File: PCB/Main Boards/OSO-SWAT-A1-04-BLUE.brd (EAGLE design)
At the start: 24.4 x 24.4 mm, 36 parts, among them J1 FH19C-9S-0.5SH_10_, U1 ATSAML22J18A-MUT, U2 MIC5365-3.3YC5-TR

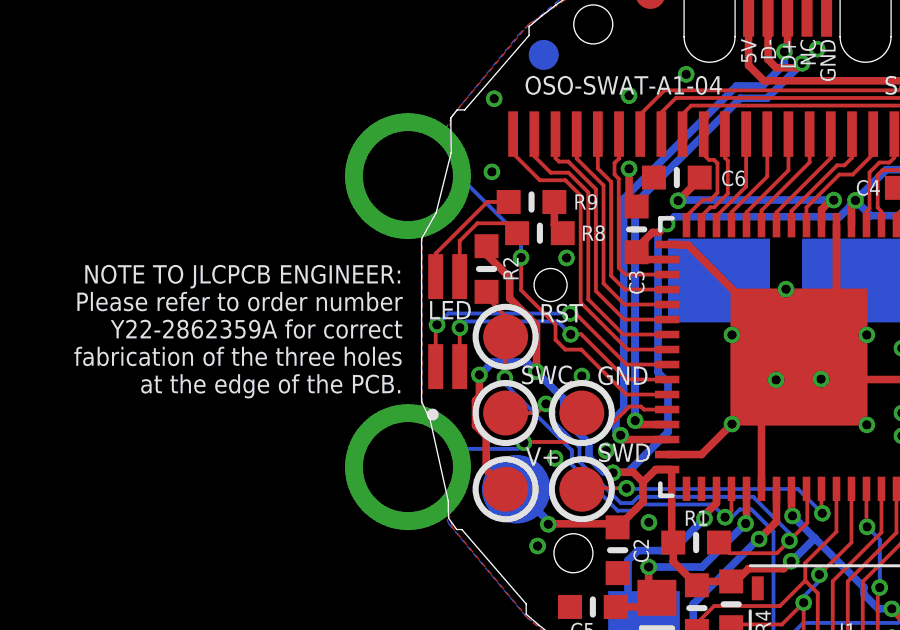
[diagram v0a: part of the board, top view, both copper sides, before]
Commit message: fix LED part number, make boards identical
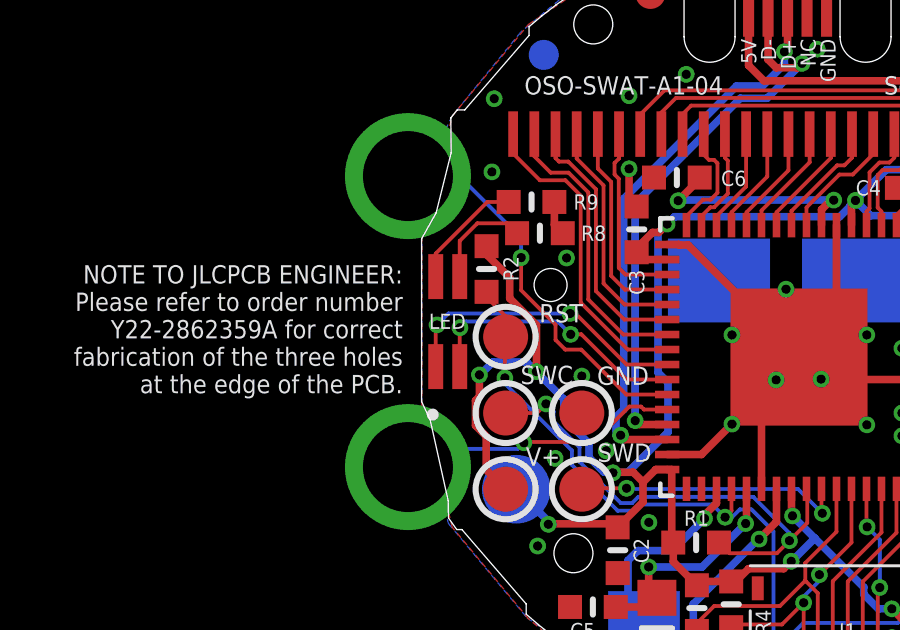
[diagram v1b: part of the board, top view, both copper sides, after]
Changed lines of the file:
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@@
 <layer number="17" name="Pads" color="2" fill="1" visible="yes" active="yes"/>
 <layer number="18" name="Vias" color="2" fill="1" visible="yes" active="yes"/>
-<layer number="19" name="Unrouted" color="6" fill="1" visible="yes" active="yes"/>
+<layer number="19" name="Unrouted" color="6" fill="1" visible="no" active="yes"/>
 <layer number="20" name="Dimension" color="15" fill="1" visible="yes" active="yes"/>
-<layer number="21" name="tPlace" color="14" fill="1" visible="yes" active="yes"/>
-<layer number="22" name="bPlace" color="13" fill="1" visible="yes" active="yes"/>
-<layer number="23" name="tOrigins" color="15" fill="1" visible="yes" active="yes"/>
-<layer number="24" name="bOrigins" color="15" fill="1" visible="yes" active="yes"/>
-<layer number="25" name="tNames" color="7" fill="1" visible="yes" active="yes"/>
-<layer number="26" name="bNames" color="7" fill="1" visible="yes" active="yes"/>
+<layer number="21" name="tPlace" color="14" fill="1" visible="no" active="yes"/>
+<layer number="22" name="bPlace" color="13" fill="1" visible="no" active="yes"/>
+<layer number="23" name="tOrigins" color="15" fill="1" visible="no" active="yes"/>
+<layer number="24" name="bOrigins" color="15" fill="1" visible="no" active="yes"/>
+<layer number="25" name="tNames" color="7" fill="1" visible="no" active="yes"/>
+<layer number="26" name="bNames" color="7" fill="1" visible="no" active="yes"/>
 <layer number="27" name="tValues" color="7" fill="1" visible="no" active="yes"/>
 <layer number="28" name="bValues" color="7" fill="1" visible="no" active="yes"/>
@@
 <layer number="37" name="tTest" color="7" fill="1" visible="no" active="yes"/>
 <layer number="38" name="bTest" color="7" fill="1" visible="no" active="yes"/>
-<layer number="39" name="tKeepout" color="4" fill="11" visible="yes" active="yes"/>
-<layer number="40" name="bKeepout" color="1" fill="11" visible="yes" active="yes"/>
-<layer number="41" name="tRestrict" color="4" fill="10" visible="yes" active="yes"/>
-<layer number="42" name="bRestrict" color="1" fill="10" visible="yes" active="yes"/>
+<layer number="39" name="tKeepout" color="4" fill="11" visible="no" active="yes"/>
+<layer number="40" name="bKeepout" color="1" fill="11" visible="no" active="yes"/>
+<layer number="41" name="tRestrict" color="4" fill="10" visible="no" active="yes"/>
+<layer number="42" name="bRestrict" color="1" fill="10" visible="no" active="yes"/>
 <layer number="43" name="vRestrict" color="2" fill="10" visible="no" active="yes"/>
 <layer number="44" name="Drills" color="7" fill="1" visible="no" active="yes"/>
@@
 <layer number="49" name="Reference" color="7" fill="1" visible="no" active="yes"/>
 <layer number="50" name="dxf" color="7" fill="1" visible="no" active="yes"/>
-<layer number="51" name="tDocu" color="15" fill="1" visible="yes" active="yes"/>
-<layer number="52" name="bDocu" color="7" fill="1" visible="yes" active="yes"/>
+<layer number="51" name="tDocu" color="15" fill="1" visible="no" active="yes"/>
+<layer number="52" name="bDocu" color="7" fill="1" visible="no" active="yes"/>
 <layer number="53" name="tGND_GNDA" color="7" fill="9" visible="no" active="no"/>
 <layer number="54" name="bGND_GNDA" color="1" fill="9" visible="no" active="no"/>
@@
 <attribute name="MF" value="Lite-On Inc." x="-11.3284" y="0" size="1.778" layer="27" rot="R90" display="off"/>
 <attribute name="MP" value="LTST-C235KGKRKT" x="-11.3284" y="0" size="1.778" layer="27" rot="R90" display="off"/>
-<attribute name="NAME" x="-11.2522" y="0.381" size="0.6096" layer="25" font="vector" ratio="18" rot="R180" align="center"/>
+<attribute name="NAME" x="-11.340009375" y="0.01056875" size="0.508" layer="25" font="vector" ratio="18" align="center"/>
 <attribute name="PACKAGE" value="1206 Lite-On" x="-11.3284" y="0" size="1.778" layer="27" rot="R90" display="off"/>
 <attribute name="PURCHASE-URL" value="https://pricing.snapeda.com/search/part/LTST-C235KGKRKT/?ref=eda" x="-11.3284" y="0" size="1.778" layer="27" rot="R90" display="off"/>

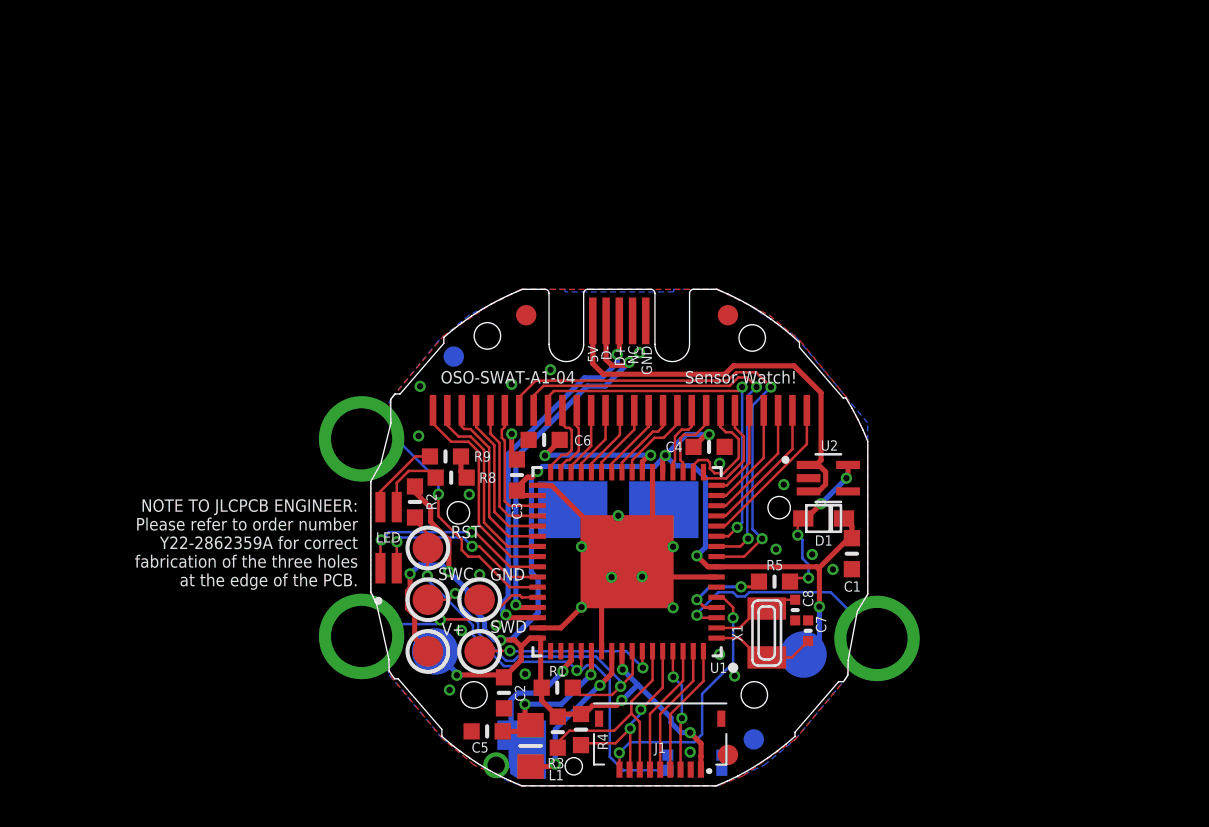
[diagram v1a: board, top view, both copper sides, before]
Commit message: tweak resistor values, move board origin to 0,0
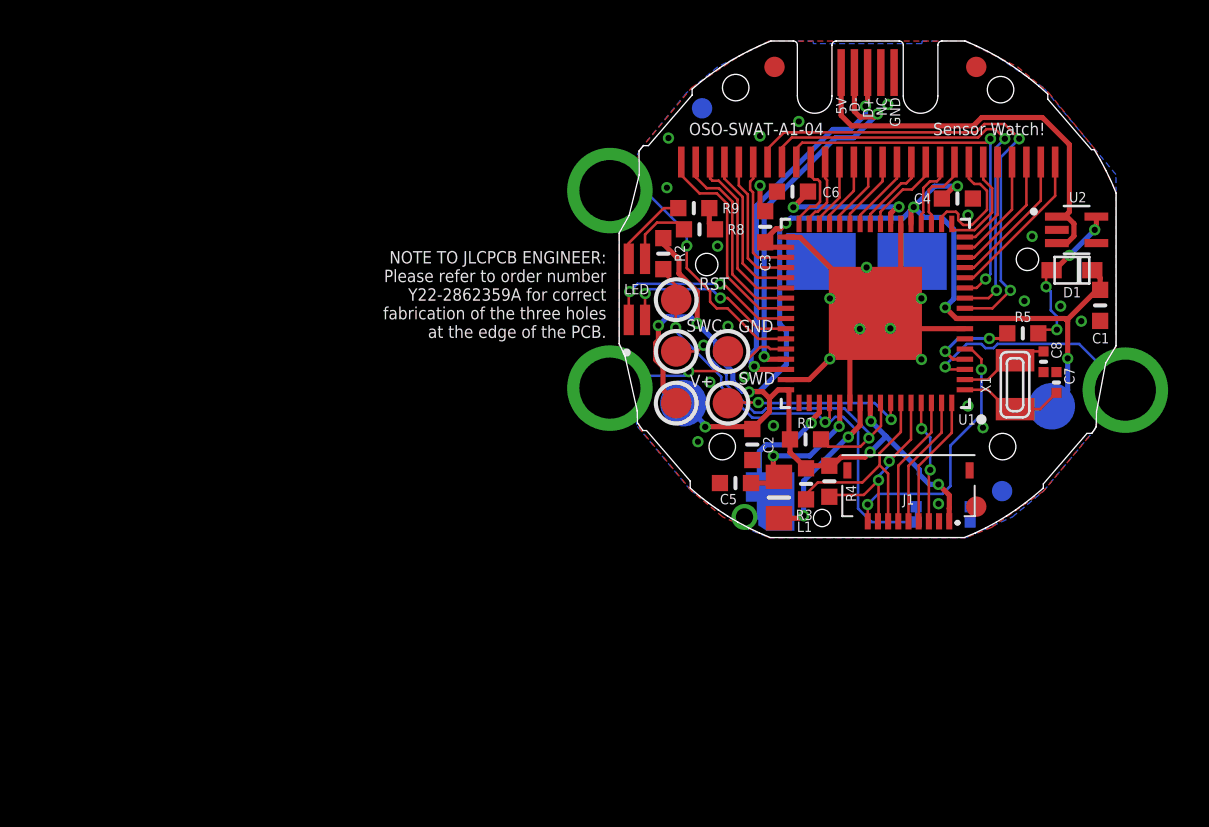
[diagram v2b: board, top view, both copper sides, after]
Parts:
- C7, C8: value TBD -> 10pf
- R8: value 100 -> 220
- R9: value 1K -> 220
- X1: value (none) -> 32.768
- moved C1 17.2 mm to (23.6, 11.4)
- moved C2 17.2 mm to (6.53, 4.57)
- moved C3 17.2 mm to (7.16, 15.3)
- moved C4 17.2 mm to (16.6, 16.6)
- moved C5 17.2 mm to (5.70, 2.68)
- moved C6 17.2 mm to (8.50, 17.0)
- moved C7 17.2 mm to (21.5, 7.62)
- moved C8 17.2 mm to (20.8, 8.64)
- moved D1 17.2 mm to (22.2, 13.1)
- moved FID1 17.2 mm to (7.62, 23.1)
- moved FID2 17.2 mm to (17.5, 23.1)
- moved FID3 17.2 mm to (17.5, 1.52)
- moved FID4 17.2 mm to (4.06, 21.1)
- moved FID6 17.2 mm to (18.8, 2.29)
- moved GND 17.2 mm to (5.33, 9.14)
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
